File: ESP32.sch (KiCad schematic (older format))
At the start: 11 parts

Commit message: Added labels
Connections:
- net MCP_INTA: now reaches U?.16 (IO13)
- net DIGITAL_1: now reaches U?.26 (IO4)
- net DIGITAL_2: now reaches U?.27 (IO16)
- net DIGITAL_3: now reaches U?.29 (IO5)
- net MCP_INTB: now reaches U?.7 (IO35)
- net DIGITAL_4: now reaches U?.8 (IO32)
- net DIGITAL_5: now reaches U?.9 (IO33)
- no-connect marks 0 -> 9
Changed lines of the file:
@@
 Wire Wire Line
 	6400 4300 6350 4300
+Text HLabel 6400 2800 2    50   Input ~ 0
+DIGITAL_1
+Text HLabel 6400 3400 2    50   Input ~ 0
+DIGITAL_2
+Text HLabel 6400 2900 2    50   Input ~ 0
+DIGITAL_3
+Text HLabel 6400 4400 2    50   Input ~ 0
+DIGITAL_4
+Text HLabel 6400 4500 2    50   Input ~ 0
+DIGITAL_5
+Text HLabel 6400 3100 2    50   Input ~ 0
+MCP_INTA
+Text HLabel 6400 4700 2    50   Input ~ 0
+MCP_INTB
+NoConn ~ 6350 4600
+NoConn ~ 5150 2600
+NoConn ~ 5150 2700
+Wire Wire Line
+	6350 4700 6400 4700
+Wire Wire Line
+	6400 4500 6350 4500
+Wire Wire Line
+	6400 4400 6350 4400
+Wire Wire Line
+	6350 3400 6400 3400
+Wire Wire Line
+	6350 3100 6400 3100
+Wire Wire Line
+	6350 2900 6400 2900
+Wire Wire Line
+	6400 2800 6350 2800
+NoConn ~ 5150 3600
+NoConn ~ 5150 3700
+NoConn ~ 5150 3800
+NoConn ~ 5150 3900
+NoConn ~ 5150 4000
+NoConn ~ 5150 4100
 $EndSCHEMATC

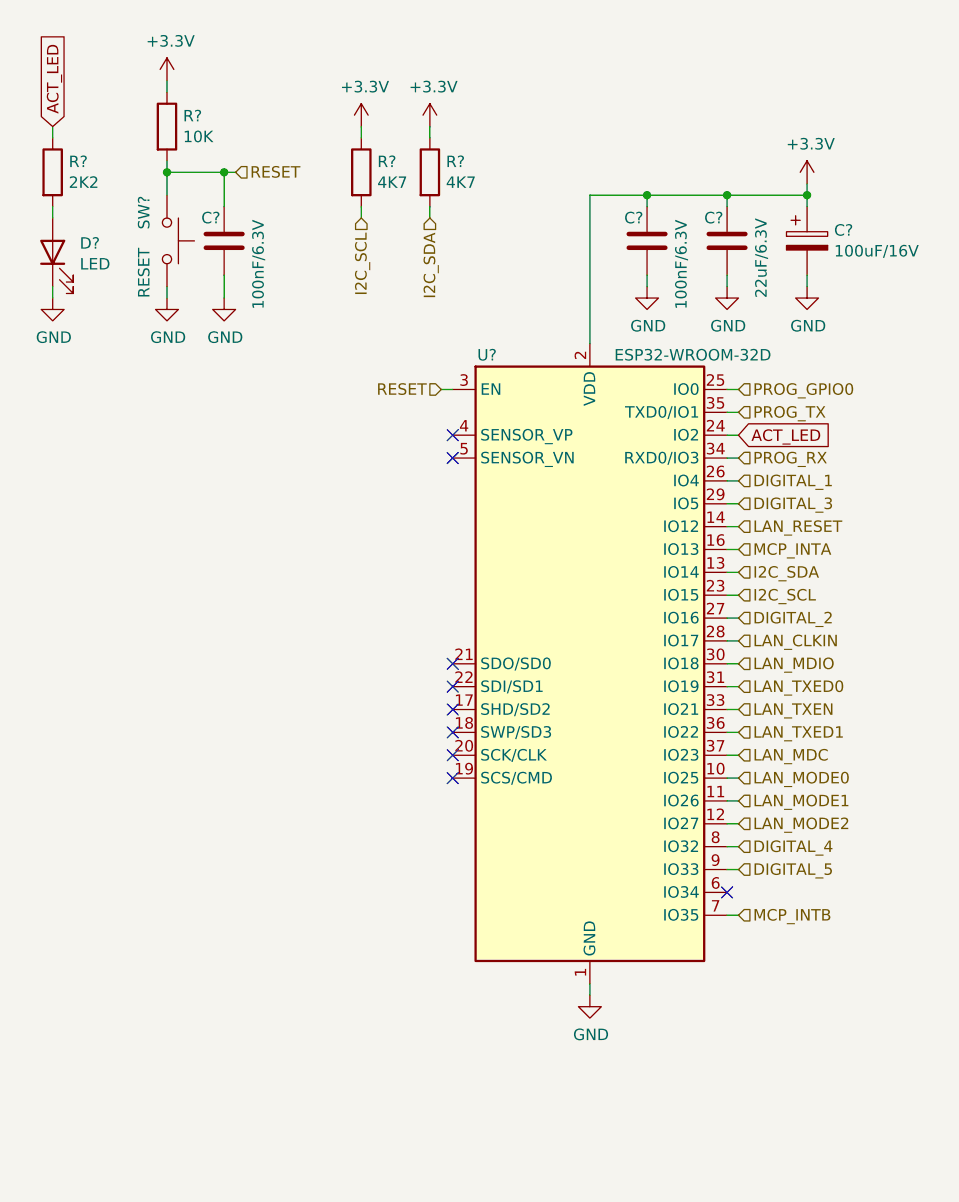
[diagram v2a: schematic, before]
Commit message: Added LAN circuit
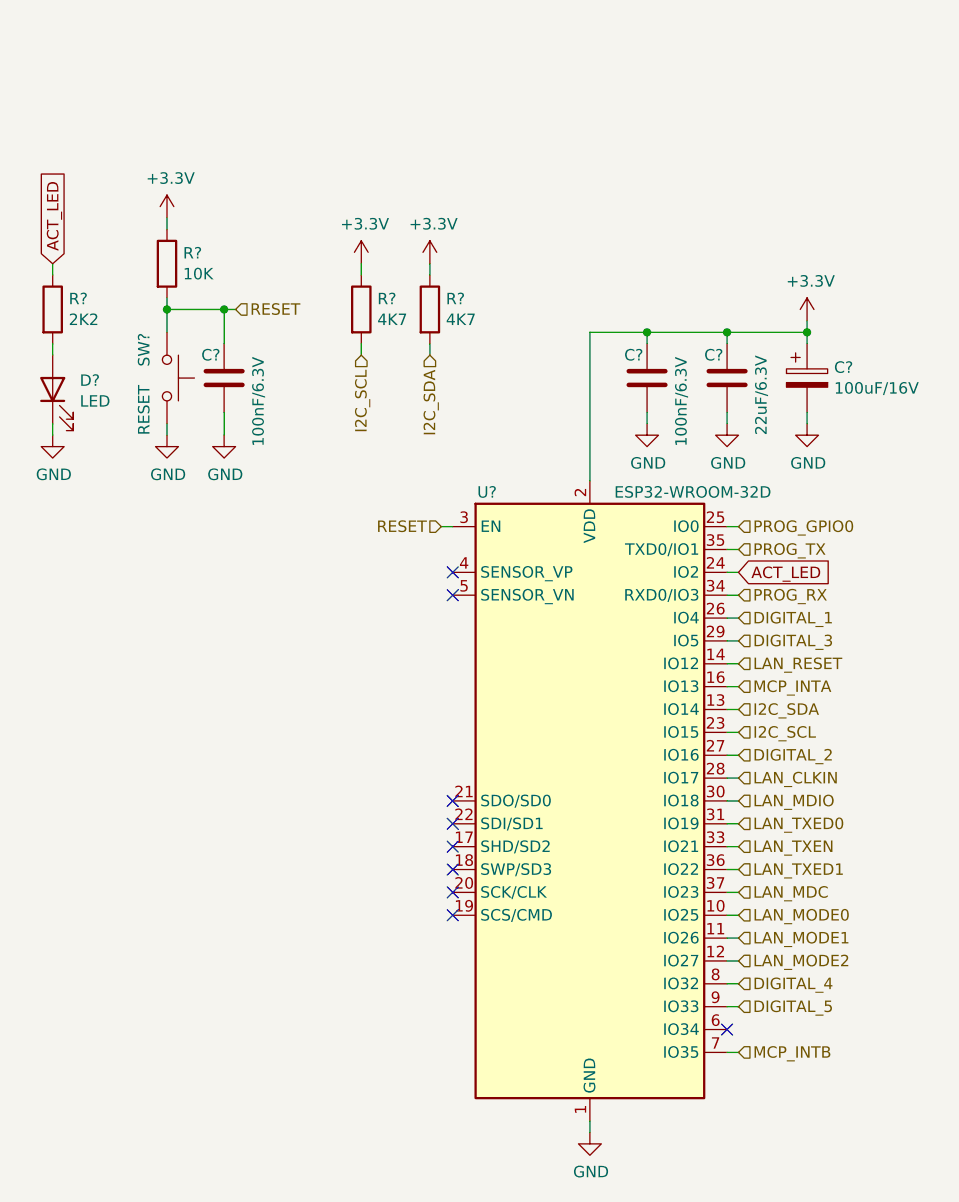
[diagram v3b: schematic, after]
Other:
- moved on the sheet: C?, D?, R?, SW?, U?

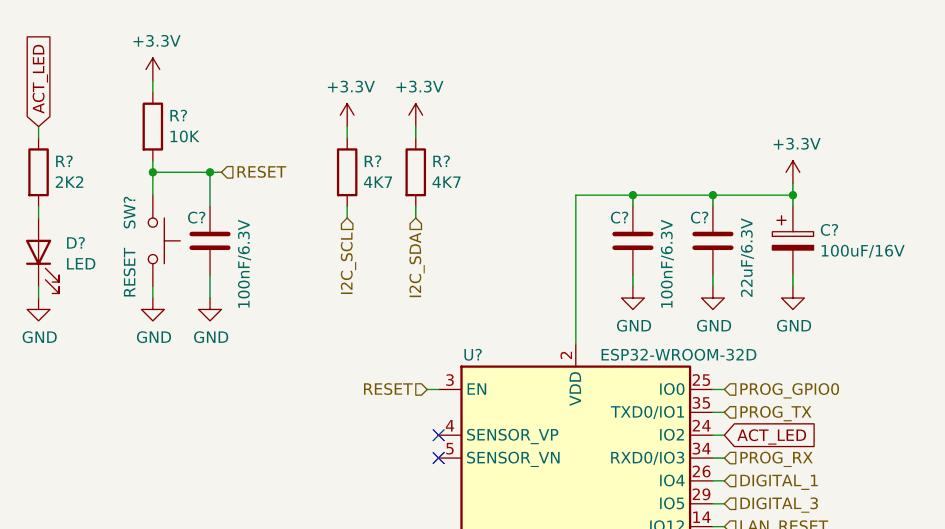
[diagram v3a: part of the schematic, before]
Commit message: Exported first net
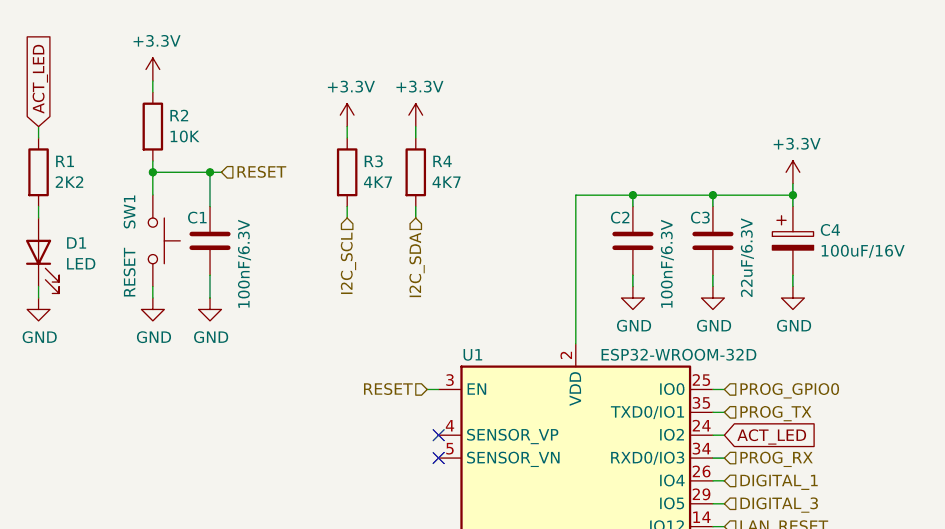
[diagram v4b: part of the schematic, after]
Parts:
- gave numbers to parts that had none: 11
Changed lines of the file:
@@
 $EndDescr
 $Comp
-L RF_Module:ESP32-WROOM-32D U?
+L RF_Module:ESP32-WROOM-32D U1
 U 1 1 6212187F
 P 5750 4200
-F 0 "U?" H 5300 5550 50  0000 C CNN
+F 0 "U1" H 5300 5550 50  0000 C CNN
 F 1 "ESP32-WROOM-32D" H 6200 5550 50  0000 C CNN
 F 2 "RF_Module:ESP32-WROOM-32" H 5750 2700 50  0001 C CNN
@@
 $EndComp
 $Comp
-L power:+3.3V #PWR?
+L power:+3.3V #PWR0101
 U 1 1 62122DDA
 P 6700 2100
-F 0 "#PWR?" H 6700 1950 50  0001 C CNN
+F 0 "#PWR0101" H 6700 1950 50  0001 C CNN
 F 1 "+3.3V" H 6715 2273 50  0000 C CNN
 F 2 "" H 6700 2100 50  0001 C CNN
@@
 $EndComp
 $Comp
-L Device:C C?
+L Device:C C2
 U 1 1 621231ED
 P 6000 2350
-F 0 "C?" H 5900 2450 50  0000 L CNN
+F 0 "C2" H 5900 2450 50  0000 L CNN
 F 1 "100nF/6.3V" V 6150 2050 50  0000 L CNN
 F 2 "Capacitor_SMD:C_0402_1005Metric" H 6038 2200 50  0001 C CNN
@@
 $EndComp
 $Comp
-L Device:C C?
+L Device:C C3
 U 1 1 621238E7
 P 6350 2350
-F 0 "C?" H 6250 2450 50  0000 L CNN
+F 0 "C3" H 6250 2450 50  0000 L CNN
 F 1 "22uF/6.3V" V 6500 2100 50  0000 L CNN
 F 2 "Capacitor_SMD:C_0402_1005Metric" H 6388 2200 50  0001 C CNN
@@
 $EndComp
 $Comp
-L Device:CP C?
+L Device:CP C4
 U 1 1 621249CB
 P 6700 2350
-F 0 "C?" H 6818 2396 50  0000 L CNN
+F 0 "C4" H 6818 2396 50  0000 L CNN
 F 1 "100uF/16V" H 6818 2305 50  0000 L CNN
 F 2 "Capacitor_SMD:CP_Elec_4x5.4" H 6738 2200 50  0001 C CNN
@@
 $EndComp
 $Comp
-L power:GND #PWR?
+L power:GND #PWR0102
 U 1 1 62125CD7
 P 6000 2550
-F 0 "#PWR?" H 6000 2300 50  0001 C CNN
+F 0 "#PWR0102" H 6000 2300 50  0001 C CNN
 F 1 "GND" H 6005 2377 50  0000 C CNN
 F 2 "" H 6000 2550 50  0001 C CNN
@@
 $EndComp
 $Comp
-L power:GND #PWR?
+L power:GND #PWR0103
 U 1 1 6212619C
 P 6350 2550
-F 0 "#PWR?" H 6350 2300 50  0001 C CNN
+F 0 "#PWR0103" H 6350 2300 50  0001 C CNN
 F 1 "GND" H 6355 2377 50  0000 C CNN
 F 2 "" H 6350 2550 50  0001 C CNN
@@
 $EndComp
 $Comp
-L power:GND #PWR?
+L power:GND #PWR0104
 U 1 1 621264D6
 P 6700 2550
-F 0 "#PWR?" H 6700 2300 50  0001 C CNN
+F 0 "#PWR0104" H 6700 2300 50  0001 C CNN
 F 1 "GND" H 6705 2377 50  0000 C CNN
 F 2 "" H 6700 2550 50  0001 C CNN
@@
 	6700 2100 6700 2150
 $Comp
-L power:GND #PWR?
+L power:GND #PWR0105
 U 1 1 62128AD9
 P 5750 5650
-F 0 "#PWR?" H 5750 5400 50  0001 C CNN
+F 0 "#PWR0105" H 5750 5400 50  0001 C CNN
 F 1 "GND" H 5755 5477 50  0000 C CNN
 F 2 "" H 5750 5650 50  0001 C CNN
@@
 RESET
 $Comp
-L Device:C C?
+L Device:C C1
 U 1 1 62129757
 P 4150 2350
-F 0 "C?" H 4050 2450 50  0000 L CNN
+F 0 "C1" H 4050 2450 50  0000 L CNN
 F 1 "100nF/6.3V" V 4300 2050 50  0000 L CNN
 F 2 "Capacitor_SMD:C_0402_1005Metric" H 4188 2200 50  0001 C CNN
@@
 $EndComp
 $Comp
-L Switch:SW_Push SW?
+L Switch:SW_Push SW1
 U 1 1 6212A51F
 P 3900 2350
-F 0 "SW?" H 3950 2250 50  0000 L CNN
+F 0 "SW1" H 3950 2250 50  0000 L CNN
 F 1 "RESET" H 3650 2250 50  0000 L CNN
 F 2 "" H 3900 2550 50  0001 C CNN
@@
 $EndComp
 $Comp
-L power:GND #PWR?
+L power:GND #PWR0106
 U 1 1 6212BE24
 P 3900 2600
-F 0 "#PWR?" H 3900 2350 50  0001 C CNN
+F 0 "#PWR0106" H 3900 2350 50  0001 C CNN
 F 1 "GND" H 3905 2427 50  0000 C CNN
 F 2 "" H 3900 2600 50  0001 C CNN
@@
 $EndComp
 $Comp
-L power:GND #PWR?
+L power:GND #PWR0107
 U 1 1 6212C38B
 P 4150 2600
-F 0 "#PWR?" H 4150 2350 50  0001 C CNN
+F 0 "#PWR0107" H 4150 2350 50  0001 C CNN
 F 1 "GND" H 4155 2427 50  0000 C CNN
 F 2 "" H 4150 2600 50  0001 C CNN
@@
 $EndComp
 $Comp
-L Device:R R?
+L Device:R R2
 U 1 1 6212C9DD
 P 3900 1850
-F 0 "R?" H 3970 1896 50  0000 L CNN
+F 0 "R2" H 3970 1896 50  0000 L CNN
 F 1 "10K" H 3970 1805 50  0000 L CNN
 F 2 "Resistor_SMD:R_0402_1005Metric" V 3830 1850 50  0001 C CNN
@@
 $EndComp
 $Comp
-L power:+3.3V #PWR?
+L power:+3.3V #PWR0108
 U 1 1 6212D33E
 P 3900 1650
-F 0 "#PWR?" H 3900 1500 50  0001 C CNN
+F 0 "#PWR0108" H 3900 1500 50  0001 C CNN
 F 1 "+3.3V" H 3915 1823 50  0000 C CNN
 F 2 "" H 3900 1650 50  0001 C CNN
@@
 ACT_LED
 $Comp
-L Device:R R?
+L Device:R R1
 U 1 1 621301FE
 P 3400 2050
-F 0 "R?" H 3470 2096 50  0000 L CNN
+F 0 "R1" H 3470 2096 50  0000 L CNN
 F 1 "2K2" H 3470 2005 50  0000 L CNN
 F 2 "Resistor_SMD:R_0402_1005Metric" V 3330 2050 50  0001 C CNN
@@
 $EndComp
 $Comp
-L Device:LED D?
+L Device:LED D1
 U 1 1 621309B2
 P 3400 2400
-F 0 "D?" V 3439 2282 50  0000 R CNN
+F 0 "D1" V 3439 2282 50  0000 R CNN
 F 1 "LED" V 3348 2282 50  0000 R CNN
 F 2 "LED_SMD:LED_0402_1005Metric" H 3400 2400 50  0001 C CNN
@@
 $EndComp
 $Comp
-L power:GND #PWR?
+L power:GND #PWR0109
 U 1 1 62131DE7
 P 3400 2600
-F 0 "#PWR?" H 3400 2350 50  0001 C CNN
+F 0 "#PWR0109" H 3400 2350 50  0001 C CNN
 F 1 "GND" H 3405 2427 50  0000 C CNN
 F 2 "" H 3400 2600 50  0001 C CNN
@@
 I2C_SDA
 $Comp
-L Device:R R?
+L Device:R R3
 U 1 1 6213451D
 P 4750 2050
-F 0 "R?" H 4820 2096 50  0000 L CNN
+F 0 "R3" H 4820 2096 50  0000 L CNN
 F 1 "4K7" H 4820 2005 50  0000 L CNN
 F 2 "Resistor_SMD:R_0402_1005Metric" V 4680 2050 50  0001 C CNN
@@
 $EndComp
 $Comp
-L Device:R R?
+L Device:R R4
 U 1 1 62134AD2
 P 5050 2050
-F 0 "R?" H 5120 2096 50  0000 L CNN
+F 0 "R4" H 5120 2096 50  0000 L CNN
 F 1 "4K7" H 5120 2005 50  0000 L CNN
 F 2 "Resistor_SMD:R_0402_1005Metric" V 4980 2050 50  0001 C CNN
@@
 $EndComp
 $Comp
-L power:+3.3V #PWR?
+L power:+3.3V #PWR0110
 U 1 1 621355DA
 P 4750 1850
-F 0 "#PWR?" H 4750 1700 50  0001 C CNN
+F 0 "#PWR0110" H 4750 1700 50  0001 C CNN
 F 1 "+3.3V" H 4765 2023 50  0000 C CNN
 F 2 "" H 4750 1850 50  0001 C CNN
@@
 $EndComp
 $Comp
-L power:+3.3V #PWR?
+L power:+3.3V #PWR0111
 U 1 1 62135A3B
 P 5050 1850
-F 0 "#PWR?" H 5050 1700 50  0001 C CNN
+F 0 "#PWR0111" H 5050 1700 50  0001 C CNN
 F 1 "+3.3V" H 5065 2023 50  0000 C CNN
 F 2 "" H 5050 1850 50  0001 C CNN

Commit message: Added to pcb
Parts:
- SW1: footprint (none) -> Button_Switch_SMD:SW_SPST_B3U-1000P
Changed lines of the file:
@@
 F 0 "SW1" H 3950 2250 50  0000 L CNN
 F 1 "RESET" H 3650 2250 50  0000 L CNN
-F 2 "" H 3900 2550 50  0001 C CNN
+F 2 "Button_Switch_SMD:SW_SPST_B3U-1000P" H 3900 2550 50  0001 C CNN
 F 3 "~" H 3900 2550 50  0001 C CNN
 	1    3900 2350

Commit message: Added lcsc part nums
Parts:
- C1, C2: value 100nF/6.3V -> 100nF/50V/10%; LCSC (none) -> C307331
- C3: value 22uF/6.3V -> 22uF/6.3V/20%; LCSC (none) -> C415703
- C4: value 100uF/16V -> 100uF/10V/20%; footprint Capacitor_SMD:CP_Elec_4x5.4 -> Capacitor_SMD:CP_Elec_5x5.4; LCSC (none) -> C96182
- D1: value LED -> LED Red; footprint LED_SMD:LED_0402_1005Metric -> LED_SMD:LED_0603_1608Metric; LCSC (none) -> C2286
- R1: value 2K2 -> 1K/1/16W/50V; LCSC (none) -> C11702
- R2: value 10K -> 10K/1/16W/50V; LCSC (none) -> C25744
- R3, R4: value 4K7 -> 4K7/1/16W/50V; LCSC (none) -> C25900
- SW1: footprint Button_Switch_SMD:SW_SPST_B3U-1000P -> Button_Switch_SMD:SW_SPST_EVPBF; LCSC (none) -> C318884
- U1: LCSC (none) -> C473012
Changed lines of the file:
@@
 F 2 "RF_Module:ESP32-WROOM-32" H 5750 2700 50  0001 C CNN
 F 3 "https://www.espressif.com/sites/default/files/documentation/esp32-wroom-32d_esp32-wroom-32u_datasheet_en.pdf" H 5450 4250 50  0001 C CNN
+F 4 "C473012" H 5750 4200 50  0001 C CNN "LCSC"
 	1    5750 4200
 	1    0    0    -1
@@
 U 1 1 621231ED
 P 6000 2350
-F 0 "C2" H 5900 2450 50  0000 L CNN
-F 1 "100nF/6.3V" V 6150 2050 50  0000 L CNN
+F 0 "C2" V 5950 2200 50  0000 L CNN
+F 1 "100nF/50V/10%" V 6150 2050 50  0000 L CNN
 F 2 "Capacitor_SMD:C_0402_1005Metric" H 6038 2200 50  0001 C CNN
 F 3 "~" H 6000 2350 50  0001 C CNN
+F 4 "C307331" H 6000 2350 50  0001 C CNN "LCSC"
 	1    6000 2350
 	1    0    0    -1
@@
 U 1 1 621238E7
 P 6350 2350
-F 0 "C3" H 6250 2450 50  0000 L CNN
-F 1 "22uF/6.3V" V 6500 2100 50  0000 L CNN
+F 0 "C3" V 6300 2200 50  0000 L CNN
+F 1 "22uF/6.3V/20%" V 6500 2100 50  0000 L CNN
 F 2 "Capacitor_SMD:C_0402_1005Metric" H 6388 2200 50  0001 C CNN
 F 3 "~" H 6350 2350 50  0001 C CNN
+F 4 "C415703" H 6350 2350 50  0001 C CNN "LCSC"
 	1    6350 2350
 	1    0    0    -1
@@
 U 1 1 621249CB
 P 6700 2350
-F 0 "C4" H 6818 2396 50  0000 L CNN
-F 1 "100uF/16V" H 6818 2305 50  0000 L CNN
-F 2 "Capacitor_SMD:CP_Elec_4x5.4" H 6738 2200 50  0001 C CNN
+F 0 "C4" V 6650 2200 50  0000 L CNN
+F 1 "100uF/10V/20%" V 6850 2050 50  0000 L CNN
+F 2 "Capacitor_SMD:CP_Elec_5x5.4" H 6738 2200 50  0001 C CNN
 F 3 "~" H 6700 2350 50  0001 C CNN
+F 4 "C96182" H 6700 2350 50  0001 C CNN "LCSC"
 	1    6700 2350
 	1    0    0    -1
@@
 U 1 1 62129757
 P 4150 2350
-F 0 "C1" H 4050 2450 50  0000 L CNN
-F 1 "100nF/6.3V" V 4300 2050 50  0000 L CNN
+F 0 "C1" V 4100 2450 50  0000 L CNN
+F 1 "100nF/50V/10%" V 4300 1950 50  0000 L CNN
 F 2 "Capacitor_SMD:C_0402_1005Metric" H 4188 2200 50  0001 C CNN
 F 3 "~" H 4150 2350 50  0001 C CNN
+F 4 "C307331" H 4150 2350 50  0001 C CNN "LCSC"
 	1    4150 2350
 	1    0    0    -1
@@
 F 0 "SW1" H 3950 2250 50  0000 L CNN
 F 1 "RESET" H 3650 2250 50  0000 L CNN
-F 2 "Button_Switch_SMD:SW_SPST_B3U-1000P" H 3900 2550 50  0001 C CNN
+F 2 "Button_Switch_SMD:SW_SPST_EVPBF" H 3900 2550 50  0001 C CNN
 F 3 "~" H 3900 2550 50  0001 C CNN
+F 4 "C318884" H 3900 2350 50  0001 C CNN "LCSC"
 	1    3900 2350
 	0    1    -1   0
@@
 U 1 1 6212C9DD
 P 3900 1850
-F 0 "R2" H 3970 1896 50  0000 L CNN
-F 1 "10K" H 3970 1805 50  0000 L CNN
+F 0 "R2" V 3900 1800 50  0000 L CNN
+F 1 "10K/1/16W/50V" H 3970 1805 50  0000 L CNN
 F 2 "Resistor_SMD:R_0402_1005Metric" V 3830 1850 50  0001 C CNN
 F 3 "~" H 3900 1850 50  0001 C CNN
+F 4 "C25744" H 3900 1850 50  0001 C CNN "LCSC"
 	1    3900 1850
 	1    0    0    -1
@@
 U 1 1 621301FE
 P 3400 2050
-F 0 "R1" H 3470 2096 50  0000 L CNN
-F 1 "2K2" H 3470 2005 50  0000 L CNN
+F 0 "R1" V 3400 2000 50  0000 L CNN
+F 1 "1K/1/16W/50V" V 3500 1900 50  0000 L CNN
 F 2 "Resistor_SMD:R_0402_1005Metric" V 3330 2050 50  0001 C CNN
 F 3 "~" H 3400 2050 50  0001 C CNN
+F 4 "C11702" H 3400 2050 50  0001 C CNN "LCSC"
 	1    3400 2050
 	1    0    0    -1
@@
 U 1 1 621309B2
 P 3400 2400
-F 0 "D1" V 3439 2282 50  0000 R CNN
-F 1 "LED" V 3348 2282 50  0000 R CNN
-F 2 "LED_SMD:LED_0402_1005Metric" H 3400 2400 50  0001 C CNN
+F 0 "D1" H 3400 2500 50  0000 R CNN
+F 1 "LED Red" H 3550 2250 50  0000 R CNN
+F 2 "LED_SMD:LED_0603_1608Metric" H 3400 2400 50  0001 C CNN
 F 3 "~" H 3400 2400 50  0001 C CNN
+F 4 "C2286" V 3400 2400 50  0001 C CNN "LCSC"
 	1    3400 2400
 	0    -1   -1   0
@@
 U 1 1 6213451D
 P 4750 2050
-F 0 "R3" H 4820 2096 50  0000 L CNN
-F 1 "4K7" H 4820 2005 50  0000 L CNN
+F 0 "R3" V 4750 2000 50  0000 L CNN
+F 1 "4K7/1/16W/50V" V 4850 1650 50  0000 L CNN
 F 2 "Resistor_SMD:R_0402_1005Metric" V 4680 2050 50  0001 C CNN
 F 3 "~" H 4750 2050 50  0001 C CNN
+F 4 "C25900" V 4750 2050 50  0001 C CNN "LCSC"
 	1    4750 2050
 	1    0    0    -1
@@
 U 1 1 62134AD2
 P 5050 2050
-F 0 "R4" H 5120 2096 50  0000 L CNN
-F 1 "4K7" H 5120 2005 50  0000 L CNN
+F 0 "R4" V 5050 2000 50  0000 L CNN
+F 1 "4K7/1/16W/50V" V 5150 1650 50  0000 L CNN
 F 2 "Resistor_SMD:R_0402_1005Metric" V 4980 2050 50  0001 C CNN
 F 3 "~" H 5050 2050 50  0001 C CNN
+F 4 "C25900" V 5050 2050 50  0001 C CNN "LCSC"
 	1    5050 2050
 	1    0    0    -1
